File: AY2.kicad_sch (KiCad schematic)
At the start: 7 parts, among them J16 DB9_Pins, J18 JOYSTICK_ON_OFF, U11 74HCT240, U9 74LS32

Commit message: Add files via upload
Corrected R58 value 470R
Added jumper for EPROM/EEPROM select
Added jumper notations
Added more buffers to clock signal
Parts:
- J18: value JOYSTICK_ON_OFF -> JS_ENABLE
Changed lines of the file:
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@@
 	(title_block
 		(title "ZX SPIDER 48 LBA")
-		(date "2026-06-25")
-		(rev "1.2")
+		(date "2026-07-12")
+		(rev "1.4")
 		(company "Drawn By LiveBoxAndy ")
 		(comment 3 "See ReadMe.MD for more details")
@@
 			)
 		)
-		(property "Value" "JOYSTICK_ON_OFF"
-			(at 62.484 102.616 0)
-			(show_name no)
-			(do_not_autoplace no)
+		(property "Value" "JS_ENABLE"
+			(at 69.85 102.616 0)
+			(show_name no)
+			(do_not_autoplace no)

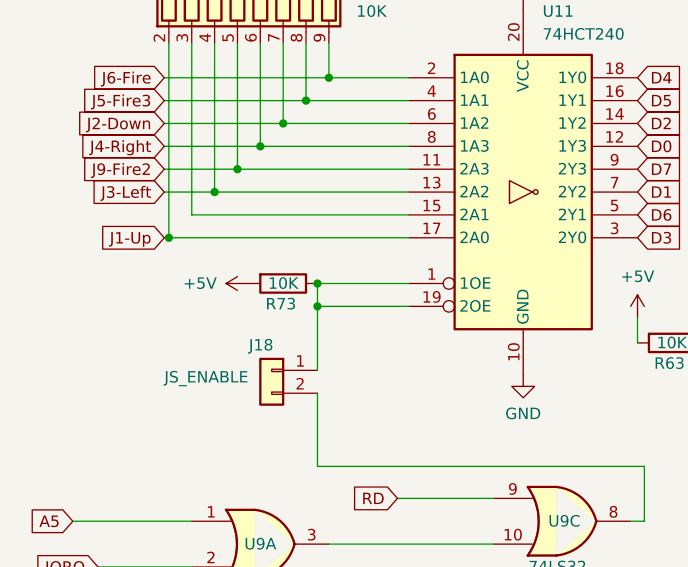
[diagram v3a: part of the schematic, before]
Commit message: Add files via upload
Updated to V1,7 Added resistor for auto RGB switching. Added resistor/zener for auto AV switching. Updated README.MD
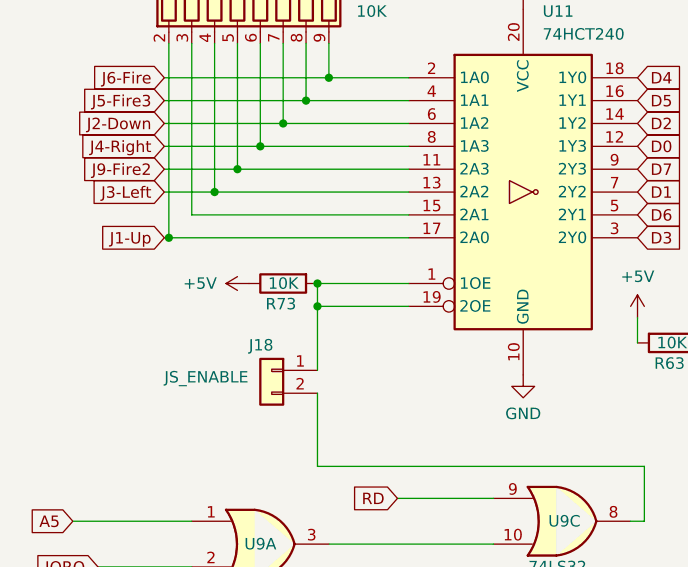
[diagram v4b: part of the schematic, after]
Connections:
- net +5V: now also R73.1; no longer R73.2
- net at J18.1 (Pin_1), U11.1 (1OE), U11.19 (2OE): now also R73.2; no longer R73.1
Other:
- moved on the sheet: R73
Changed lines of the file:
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@@
 	(title_block
 		(title "ZX SPIDER 48 LBA")
-		(date "2026-08-22")
-		(rev "1.6")
+		(date "2026-09-20")
+		(rev "1.7")
 		(company "Drawn By LiveBoxAndy ")
 		(comment 3 "See README.MD for more details")
@@
 	(symbol
 		(lib_id "Device:R")
-		(at 83.058 92.202 270)
+		(at 83.058 92.202 90)
+		(mirror x)
 		(unit 1)
 		(body_style 1)
